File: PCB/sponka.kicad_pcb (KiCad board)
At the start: 2 copper layers, 87.1 x 13.3 mm, 31 parts, among them J1 Conn_01x03_Pin, J2 USB_C_Receptacle_USB2.0_14P, J3 Conn_01x02_Socket, J4 Conn_01x05_Pin, SW1 SW_Push, SW2 SW_SPDT, U1 CH32V003FxUx, U2 TP4057, U3 AP2127K-3.3

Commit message: Made smol :) Anyway, this is just WIP, still working on it
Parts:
- removed D1, D2, D3, D4, D5, D6: WS2812B, LED_SMD:LED_WS2812B_PLCC4_5.0x5.0mm_P3.2mm
- removed D_STDBY1: LED, LED_SMD:LED_0603_1608Metric
- added LED1: WS2812B-MINI, sponka:LED-SMD_4P-L3.5-W3.5-TL_WS2812B, F.Cu at (97.9, 82.4)
- added LED2: WS2812B-MINI, sponka:LED-SMD_4P-L3.5-W3.5-TL_WS2812B, F.Cu at (104.4, 82.4)
- added LED3: WS2812B-MINI, sponka:LED-SMD_4P-L3.5-W3.5-TL_WS2812B, F.Cu at (110.9, 82.4)
- added LED4: WS2812B-MINI, sponka:LED-SMD_4P-L3.5-W3.5-TL_WS2812B, F.Cu at (117.4, 82.4)
- added LED5: WS2812B-MINI, sponka:LED-SMD_4P-L3.5-W3.5-TL_WS2812B, F.Cu at (123.9, 82.4)
- added LED6: WS2812B-MINI, sponka:LED-SMD_4P-L3.5-W3.5-TL_WS2812B, F.Cu at (130.4, 82.4)
- moved J3 53.6 mm to (131.4, 99.0), turned to 90 degrees
- moved R8 53.5 mm to (122.6, 103.2), turned to 180 degrees
- moved C5 52.0 mm to (121.0, 102.5), turned to -90 degrees
- moved U3 52.0 mm to (123.5, 101.0)
- moved SW2 52.0 mm to (130.0, 104.6)
- moved R7 51.6 mm to (124.5, 103.2)
- moved J1 25.8 mm to (118.7, 105.4)
- moved SW1 7.78 mm to (112.5, 104.6), turned to 180 degrees
- moved J4 6.24 mm to (123.0, 97.6)
- moved C2 3.90 mm to (116.1, 103.9)
- moved C1 2.45 mm to (118.0, 103.9), turned to 180 degrees
- moved R1 1.59 mm to (111.0, 100.3), turned to 180 degrees
- moved D_CHRG1 1.56 mm to (115.9, 97.7), turned to -90 degrees
- moved R9 1.48 mm to (112.0, 101.3)
- moved C3 0.89 mm to (112.8, 100.3)
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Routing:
- net /Power management/BATT_DIV: track 66.8 -> 7.62 mm
- net Net-(J3-Pin_2): track 83.5 -> 27.5 mm
- net +3V3: track 93.7 -> 53.0 mm
- net Net-(J1-Pin_2): track 33.7 -> 11.2 mm
- net Net-(D1-DOUT): track 14.3 -> 0.00 mm
- net Net-(D5-DOUT): track 14.3 -> 0.00 mm
- net Net-(D4-DOUT): track 14.3 -> 0.00 mm
- net Net-(D3-DOUT): track 14.3 -> 0.00 mm
- net Net-(D2-DOUT): track 14.3 -> 0.00 mm
- net Net-(LED5-DOUT): track 0.00 -> 10.5 mm, vias 0 -> 2
- net Net-(LED3-DOUT): track 0.00 -> 10.5 mm, vias 0 -> 2
- net Net-(LED2-DOUT): track 0.00 -> 10.5 mm, vias 0 -> 2
- net Net-(LED1-DOUT): track 0.00 -> 10.5 mm, vias 0 -> 2
- net Net-(LED4-DOUT): track 0.00 -> 10.5 mm, vias 0 -> 2
- net /LED Row/Row_DIN: track 12.8 -> 4.37 mm
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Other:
- board size 87.1 x 13.3 mm -> 87.1 x 10.9 mm
- board text removed: "BTN"
- board text removed: "CHRG"
- board text removed: "RISC-V MCU"
- board text removed: "STBY"
- board text removed: "USB-C"

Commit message: Progress update
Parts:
- J3: footprint sponka:HDR-SMD_2P-P2.54-H-M-W13.3-N -> Connector_JST:JST_PH_B2B-PH-SM4-TB_1x02-1MP_P2.00mm_Vertical
- SW1: footprint Button_Switch_SMD:SW_SPST_B3U-1000P-B -> Button_Switch_SMD:SW_SPST_B3U-1000P
- moved LED1 47.2 mm to (142.2, 98.3), turned to 180 degrees
- moved LED2 47.2 mm to (148.8, 98.3), turned to 180 degrees
- moved LED3 47.2 mm to (155.2, 98.3), turned to 180 degrees
- moved LED4 43.6 mm to (155.0, 104.3)
- moved LED5 33.0 mm to (148.5, 104.3)
- moved LED6 24.8 mm to (142.0, 104.3)
- moved SW2 3.40 mm to (126.6, 104.7)
- moved R7 3.21 mm to (121.3, 103.5), turned to -90 degrees
- moved J3 3.01 mm to (133.8, 100.8), turned to 0 degrees
- moved R8 2.26 mm to (120.3, 103.5), turned to 90 degrees
- moved C5 1.54 mm to (121.3, 101.0), turned to 90 degrees
- moved U3 0.66 mm to (123.9, 100.5)
- moved J4 0.34 mm to (123.0, 97.2)
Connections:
- SW2 pad : (no net) -> GND
- U2 pad 5: Net-(D_STDBY1-K) -> unconnected-(U2-STDBY-Pad5)
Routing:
- net GND: track 69.4 -> 47.6 mm, vias 8 -> 19
- net /LED Row/Row_DIN: track 4.37 -> 25.7 mm
- net +3V3: track 53.0 -> 64.2 mm
- net Net-(J3-Pin_2): track 27.5 -> 35.1 mm
- net Net-(LED5-DOUT): track 10.5 -> 3.96 mm, vias 2 -> 0
- net Net-(LED4-DOUT): track 10.5 -> 3.96 mm, vias 2 -> 0
- net Net-(LED2-DOUT): track 10.5 -> 3.96 mm, vias 2 -> 0
- net Net-(LED1-DOUT): track 10.5 -> 3.96 mm, vias 2 -> 0
- net Net-(LED3-DOUT): track 10.5 -> 6.95 mm, vias 2 -> 0
- net Net-(U2-PROG): track 0.00 -> 1.71 mm
- net /Power management/BATT_DIV: track 7.62 -> 9.13 mm
- net Net-(SW2-C): track 17.8 -> 16.6 mm
- net /RX/SDA: track 6.58 -> 7.13 mm
- added copper zone on F.Cu, net GND
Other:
- board size 87.1 x 10.9 mm -> 59.3 x 10.9 mm
- board text added: "D"
- board text added: "RTS"
- board text added: "RX"
- board text added: "TX"
- board text removed: "R"
- board text removed: "RS"
- board text removed: "SWITCH"
- board text removed: "T"

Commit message: Probably done?
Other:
- board text added: "Flip for help"
- board text added: "ON"
- board text added: "RISC-V"
- board text added: "USB-C"
- board text removed: "BAT"
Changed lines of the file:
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@@
 		(attr smd)
 		(fp_line
-			(start -4.085 -4.36)
-			(end 4.085 -4.36)
-			(stroke
-				(width 0.12)
-				(type solid)
-			)
-			(layer "F.SilkS")
-		)
-		(fp_line
-			(start -4.085 -3.51)
-			(end -4.085 -4.36)
-			(stroke
-				(width 0.12)
-				(type solid)
-			)
-			(layer "F.SilkS")
-		)
-		(fp_line
-			(start -4.085 0.01)
-			(end -4.085 0.86)
-			(stroke
-				(width 0.12)
-				(type solid)
-			)
-			(layer "F.SilkS")
-		)
-		(fp_line
-			(start -4.085 0.86)
-			(end -1.76 0.86)
-			(stroke
-				(width 0.12)
-				(type solid)
-			)
-			(layer "F.SilkS")
-		)
-		(fp_line
-			(start -1.76 0.86)
-			(end -1.76 3.25)
-			(stroke
-				(width 0.12)
-				(type solid)
-			)
-			(layer "F.SilkS")
-		)
-		(fp_line
-			(start 4.085 -4.36)
-			(end 4.085 -3.51)
-			(stroke
-				(width 0.12)
-				(type solid)
-			)
-			(layer "F.SilkS")
-		)
-		(fp_line
-			(start 4.085 0.01)
-			(end 4.085 0.86)
-			(stroke
-				(width 0.12)
-				(type solid)
-			)
-			(layer "F.SilkS")
-		)
-		(fp_line
-			(start 4.085 0.86)
-			(end 1.76 0.86)
-			(stroke
-				(width 0.12)
-				(type solid)
-			)
-			(layer "F.SilkS")
-		)
-		(fp_line
 			(start -4.7 -4.75)
 			(end -4.7 3.75)
@@
 		(attr smd)
 		(fp_line
-			(start -1.485 0.735)
-			(end 0.8 0.735)
-			(stroke
-				(width 0.12)
-				(type solid)
-			)
-			(layer "F.SilkS")
-		)
-		(fp_line
-			(start -1.485 -0.735)
-			(end -1.485 0.735)
-			(stroke
-				(width 0.12)
-				(type solid)
-			)
-			(layer "F.SilkS")
-		)
-		(fp_line
-			(start 0.8 -0.735)
-			(end -1.485 -0.735)
-			(stroke
-				(width 0.12)
-				(type solid)
-			)
-			(layer "F.SilkS")
-		)
-		(fp_line
 			(start -1.48 0.73)
 			(end -1.48 -0.73)
@@
 		)
 	)
-	(gr_text "La Sponka"
-		(at 143.6 86.05 0)
+	(gr_text "WS2812B"
+		(at 159.1 104.9 90)
 		(layer "F.SilkS")
 		(effects
 			(font
-				(size 1.2 1.2)
-				(thickness 0.3)
+				(size 1 1)
+				(thickness 0.2)
 				(bold yes)
 			)
@@
 		)
 	)
-	(gr_text "-"
-		(at 116.45 105 0)
+	(gr_text "by Vesek"
+		(at 150.25 102 0)
 		(layer "F.SilkS")
 		(effects
@@
 		)
 	)
-	(gr_text "BAT"
-		(at 137.6 105 90)
+	(gr_text "RISC-V"
+		(at 119.125 99.4 0)
 		(layer "F.SilkS")
 		(effects
 			(font
-				(size 1 1)
+				(size 0.9 0.9)
 				(thickness 0.2)
 				(bold yes)
 			)
-			(justify left bottom)
+			(justify bottom)
 		)
 	)
-	(gr_text "by Vesek"
-		(at 158.4 85.9 0)
+	(gr_text "-"
+		(at 116.45 105 0)
 		(layer "F.SilkS")
 		(effects
@@
 		)
 	)
-	(gr_text "WS2812B"
-		(at 169.65 99.1 0)
+	(gr_text "ON"
+		(at 126.9 102.2 0)
 		(layer "F.SilkS")
 		(effects
@@
 		)
 	)
+	(gr_text "Flip\nfor help"
+		(at 139 105.95 0)
+		(layer "F.SilkS")
+		(effects
+			(font
+				(size 1 1)
+				(thickness 0.2)
+				(bold yes)
+			)
+			(justify right bottom)
+		)
+	)
+	(gr_text "USB-C"
+		(at 113.1 102.95 0)
+		(layer "F.SilkS")
+		(effects
+			(font
+				(size 0.9 0.8)
+				(thickness 0.2)
+				(bold yes)
+			)
+			(justify bottom)
+		)
+	)
+	(gr_text "La Sponka"
+		(at 140.15 102 0)
+		(layer "F.SilkS")
+		(effects
+			(font
+				(size 1.2 1.2)
+				(thickness 0.3)
+				(bold yes)
+			)
+			(justify left bottom)
+		)
+	)
 	(segment
 		(start 146.89 103.43)
@@
 	)
 	(segment
+		(start 133.8 99.25)
+		(end 132.85 100.2)
+		(width 0.4)
+		(layer "F.Cu")
+		(net 2)
+	)
+	(segment
 		(start 111.51 100.3)
 		(end 112.37 100.3)
@@
 	)
 	(segment
-		(start 132.85 100.5)
-		(end 133.75 99.6)
-		(width 0.4)
-		(layer "F.Cu")
-		(net 2)
-	)
-	(segment
 		(start 117.675 102.75)
 		(end 117.675 101.7)
@@
 	)
 	(segment
+		(start 132.85 100.2)
+		(end 132.85 101.25)
+		(width 0.4)
+		(layer "F.Cu")
+		(net 2)
+	)
+	(segment
 		(start 117.675 103.695)
 		(end 117.675 102.75)
@@
 	)
 	(segment
-		(start 132.85 101.25)
-		(end 132.85 100.5)
-		(width 0.4)
-		(layer "F.Cu")
-		(net 2)
-	)
-	(segment
 		(start 109.04 97.72)
 		(end 108.355 97.72)
@@
 	)
 	(via
-		(at 133.75 99.6)
+		(at 133.8 99.25)
 		(size 0.6)
 		(drill 0.3)
@@
 		)
 	)
-	(group ""
-		(members "598cf0ff-a2bf-4c24-b272-a4f7a81e5f31" "89a40135-e1ff-4b9a-a54b-37ca4873dd33")
-	)
 )

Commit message: New design WIP
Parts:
- removed LED6: WS2812B-MINI, sponka:LED-SMD_4P-L3.5-W3.5-TL_WS2812B
- moved R9 50.6 mm to (61.7, 105.8), turned to 0 degrees
- moved SW1 49.3 mm to (63.2, 102.6), turned to 0 degrees
- moved J4 45.2 mm to (79.2, 108.1), turned to 0 degrees
- moved SW2 44.9 mm to (82.6, 95.6)
- moved R7 37.2 mm to (89.6, 84.1), turned to 0 degrees
- moved R8 35.3 mm to (89.6, 86.1), turned to 0 degrees
- moved C5 34.3 mm to (89.6, 88.0), turned to 0 degrees
- moved U3 34.2 mm to (90.1, 95.0), turned to 0 degrees
- moved C1 33.1 mm to (85.1, 107.8), turned to 0 degrees
- moved C2 31.5 mm to (85.1, 109.8), turned to 0 degrees
- moved LED1 30.0 mm to (112.4, 101.3), turned to 0 degrees
- moved LED5 27.8 mm to (176.2, 101.3)
- moved LED2 20.6 mm to (128.4, 101.3), turned to 0 degrees
- moved J1 15.5 mm to (104.0, 110.3), turned to -90 degrees
- moved LED3 11.4 mm to (144.3, 101.3), turned to 0 degrees
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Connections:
- J3 pad MP: (no net) -> GND
- LED5 pad 2: Net-(LED5-DOUT) -> unconnected-(LED5-DOUT-Pad2)
- SW2 pad : GND -> (no net)
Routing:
- net +3V3: track 64.2 -> 0.00 mm
- net /LED Row/Row_DIN: track 25.7 -> 0.00 mm, vias 2 -> 0
- net Net-(SW2-C): track 16.6 -> 0.00 mm
- net Net-(J1-Pin_2): track 11.2 -> 0.00 mm, vias 2 -> 0
- net /TX: track 9.42 -> 0.00 mm
- net /Power management/BATT_DIV: track 9.13 -> 0.00 mm, vias 2 -> 0
- net GND: track 48.0 -> 40.6 mm, vias 19 -> 5
- net Net-(J3-Pin_2): track 35.1 -> 27.7 mm, vias 2 -> 0
- net /RX/SDA: track 7.13 -> 0.00 mm
- net Net-(LED3-DOUT): track 6.95 -> 0.00 mm
- net Net-(D_CHRG1-K): track 8.02 -> 1.69 mm, vias 2 -> 0
- net /Power management/USB_DN: track 6.11 -> 0.00 mm
- net /Power management/USB_DP: track 5.84 -> 0.00 mm
- net /Power management/VBUS: track 17.5 -> 12.6 mm
- net /RTS/SCL: track 4.71 -> 0.00 mm
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- removed copper zone on F.Cu, net GND
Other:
- board size 59.3 x 10.9 mm -> 87.2 x 10.9 mm

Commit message: Ma favorite design yet!
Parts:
- J3: footprint Connector_JST:JST_PH_B2B-PH-SM4-TB_1x02-1MP_P2.00mm_Vertical -> Connector_JST:JST_ACH_BM02B-ACHSS-GAN-ETF_1x02-1MP_P1.20mm_Vertical
- moved R9 87.7 mm to (149.1, 98.2), turned to 180 degrees
- moved J4 77.3 mm to (156.4, 105.0), turned to 90 degrees
- moved C1 68.2 mm to (153.1, 101.8), turned to 180 degrees
- moved J1 55.5 mm to (158.2, 98.1), turned to 90 degrees
- moved SW1 55.5 mm to (118.6, 99.8), turned to 90 degrees
- moved R7 38.1 mm to (125.1, 97.9)
- moved R8 37.7 mm to (125.1, 98.8), turned to 180 degrees
- moved SW2 37.7 mm to (119.2, 104.6)
- moved C5 37.1 mm to (124.6, 100.2), turned to 90 degrees
- moved C2 33.4 mm to (116.5, 98.3), turned to -90 degrees
- moved U3 32.7 mm to (122.5, 100.1), turned to 90 degrees
- moved U1 31.0 mm to (152.1, 99.2)
- moved C3 11.8 mm to (109.7, 97.0), turned to -90 degrees
- moved R3 9.45 mm to (116.0, 99.7), turned to 180 degrees
- moved R4 8.95 mm to (116.0, 100.6), turned to 180 degrees
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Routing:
- net +3V3: track 0.00 -> 87.2 mm
- net /LED Row/Row_DIN: track 0.00 -> 48.8 mm, vias 0 -> 2
- net Net-(U1-PD7): track 0.00 -> 41.4 mm, vias 0 -> 2
- net /Power management/USB_DN: track 0.00 -> 38.0 mm, vias 0 -> 2
- net /Power management/USB_DP: track 0.00 -> 35.1 mm, vias 0 -> 2
- net GND: track 40.6 -> 69.7 mm, vias 5 -> 20
- net /Power management/BATT_DIV: track 0.00 -> 28.9 mm, vias 0 -> 2
- net Net-(LED3-DOUT): track 0.00 -> 15.0 mm, vias 0 -> 2
- net Net-(LED1-DOUT): track 0.00 -> 14.4 mm, vias 0 -> 2
- net Net-(LED4-DOUT): track 0.00 -> 13.7 mm
- net Net-(LED2-DOUT): track 0.00 -> 13.7 mm
- net Net-(SW2-C): track 0.00 -> 12.6 mm
- net Net-(J2-D+-PadA6): track 2.64 -> 14.7 mm, vias 0 -> 2
- net Net-(J2-D--PadA7): track 2.73 -> 14.2 mm, vias 0 -> 2
- net /RTS/SCL: track 0.00 -> 9.02 mm, vias 0 -> 2
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- added copper zone on F.Cu, net GND

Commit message: Update silkscreen
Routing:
- net GND: track 69.7 -> 71.8 mm
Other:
- board text added: "BAT"
- board text added: "Button - PD7"
- board text added: "RISC-V MCU"
- board text removed: "Flip for help"
- board text removed: "ON"
- board text removed: "RISC-V"

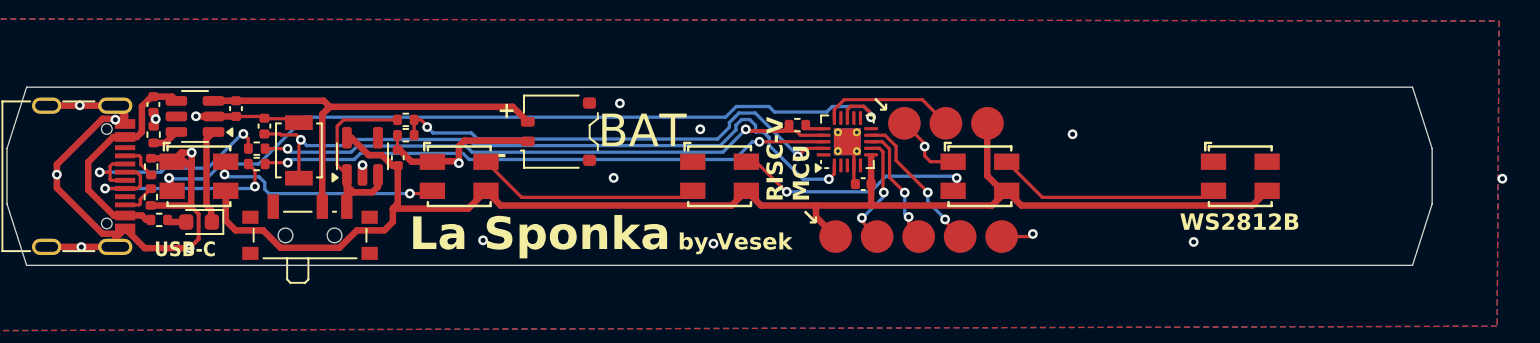
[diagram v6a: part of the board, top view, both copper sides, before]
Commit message: Update the backside
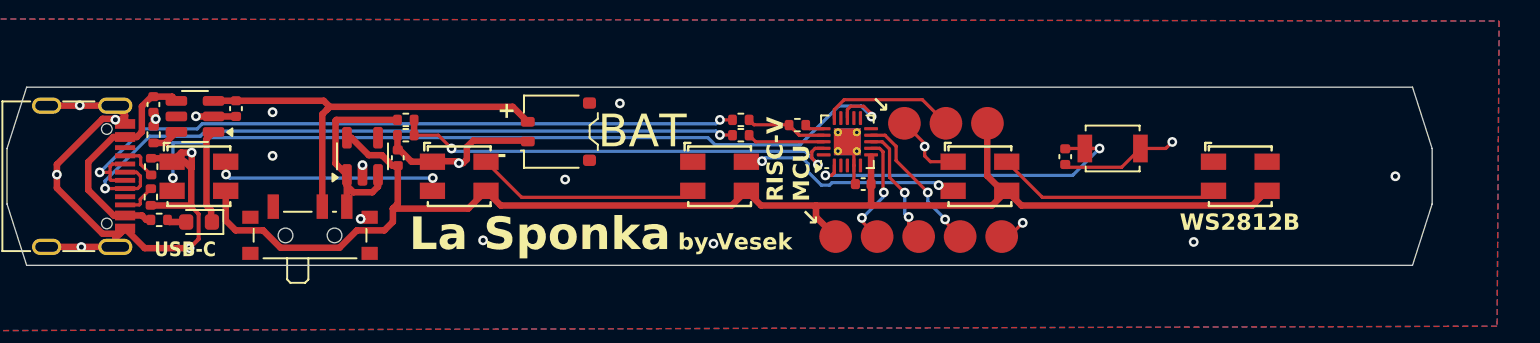
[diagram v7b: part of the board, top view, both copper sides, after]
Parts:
- moved SW1 49.8 mm to (168.3, 99.7), turned to 0 degrees
- moved C2 49.0 mm to (165.4, 100.2), turned to 90 degrees
- moved R3 29.7 mm to (145.6, 97.9)
- moved R4 29.7 mm to (145.6, 98.8)
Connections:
- net Net-(J2-D+-PadA6) renamed /Power management/DP
- net Net-(J2-D--PadA7) renamed /Power management/DN
- J3 pad MP: GND -> (no net)
- SW2 pad : (no net) -> GND
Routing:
- net /Power management/USB_DN: track 38.0 -> 4.95 mm, vias 2 -> 0
- net /Power management/USB_DP: track 35.1 -> 4.73 mm, vias 2 -> 0
- net /Power management/DP: track 14.7 -> 44.2 mm
- net /Power management/DN: track 14.2 -> 43.4 mm
- net Net-(U1-PD7): track 41.4 -> 21.5 mm
- net GND: track 71.8 -> 75.1 mm, vias 20 -> 22
- net Net-(LED3-DOUT): track 15.0 -> 14.0 mm
- net /LED Row/Row_DIN: track 48.8 -> 49.7 mm
- net Net-(LED1-DOUT): track 14.4 -> 13.5 mm
- net /Power management/BATT_DIV: track 28.9 -> 28.2 mm

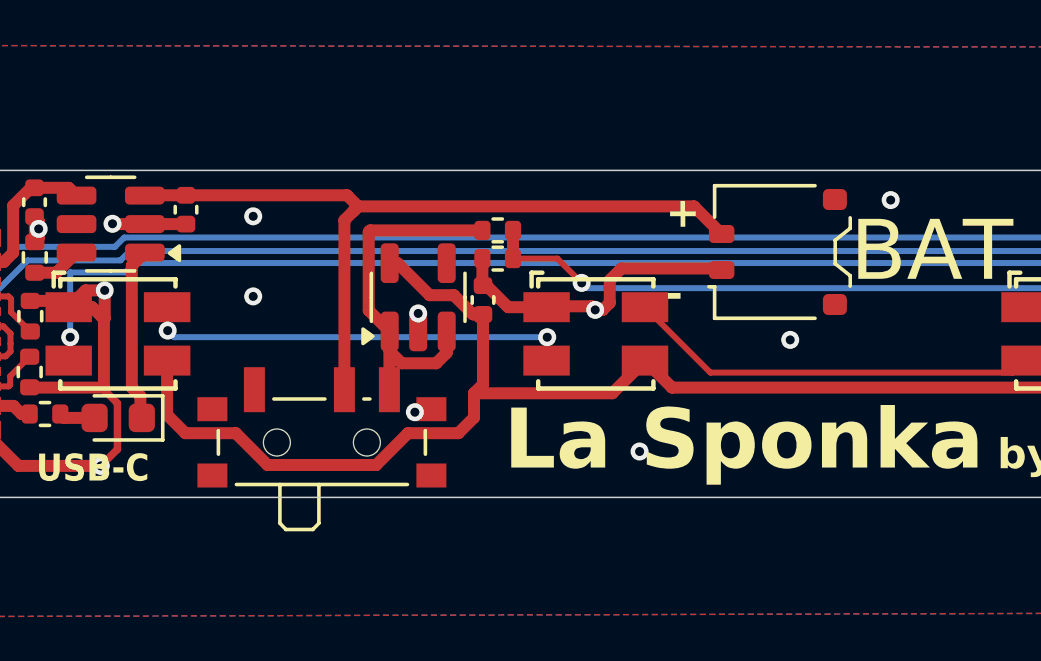
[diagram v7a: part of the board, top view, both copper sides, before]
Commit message: Change the battery connector resolve issues
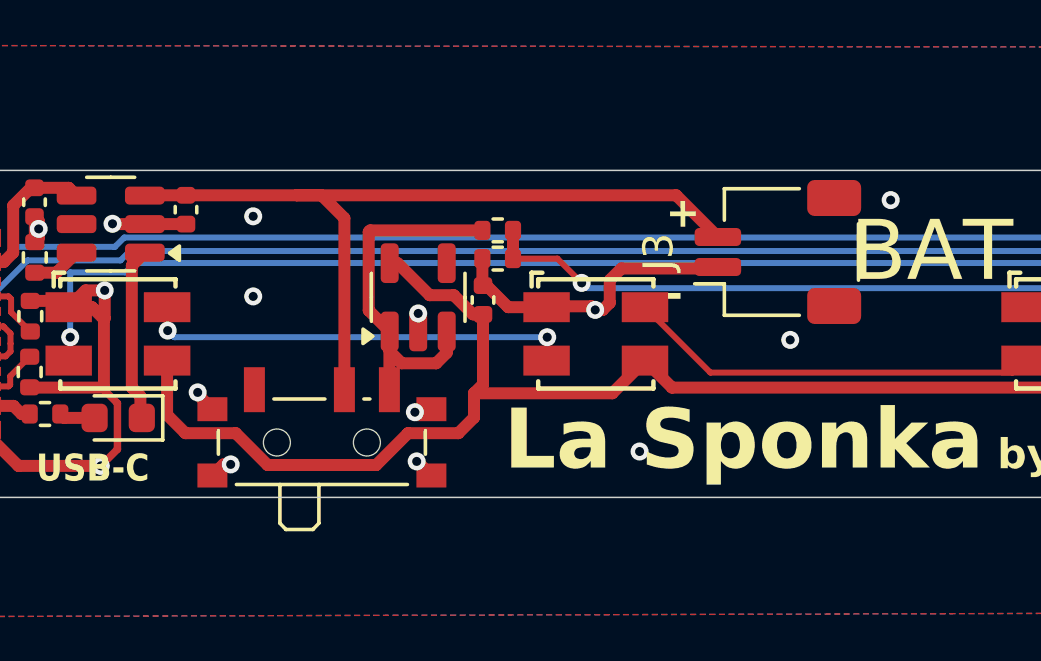
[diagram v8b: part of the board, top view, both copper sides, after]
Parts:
- J3: footprint Connector_JST:JST_ACH_BM02B-ACHSS-GAN-ETF_1x02-1MP_P1.20mm_Vertical -> Connector_JST:JST_SH_SM02B-SRSS-TB_1x02-1MP_P1.00mm_Horizontal
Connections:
- J3 pad MP: (no net) -> GND
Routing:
- net GND: track 75.1 -> 77.3 mm, vias 22 -> 25
- net Net-(J3-Pin_2): track 26.3 -> 27.3 mm
